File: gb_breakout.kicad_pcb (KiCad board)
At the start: 2 copper layers, 51 x 60.7 mm, 14 parts, among them IC1 74ALVC164245DGG_11, IC2 74ALVC164245DGG_11, J1 Conn_02x16_Counter_Clockwise, U1 Cartridge_Bus

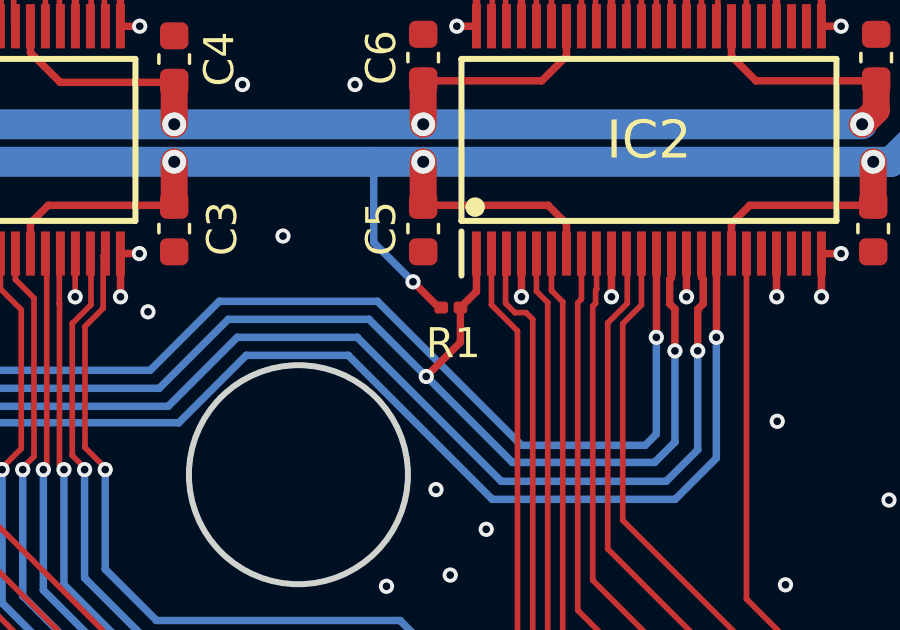
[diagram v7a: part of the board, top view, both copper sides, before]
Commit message: change 0201 resistor to 0402, woops
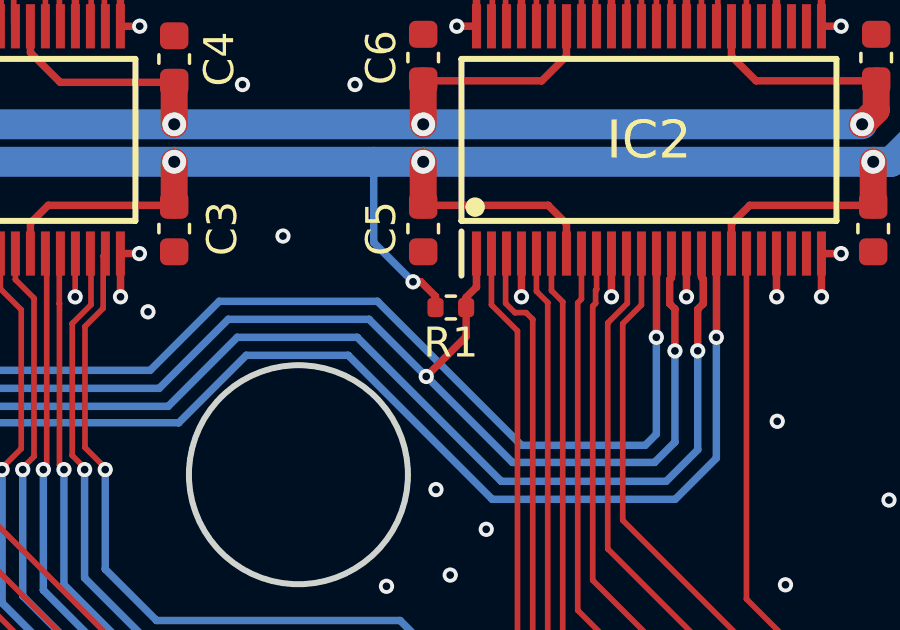
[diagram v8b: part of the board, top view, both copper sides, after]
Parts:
- R1: footprint Resistor_SMD:R_0201_0603Metric -> Resistor_SMD:R_0402_1005Metric
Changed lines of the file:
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@@
     (pad_to_mask_clearance 0)
     (pcbplotparams
-      (layerselection 0x00010fc_ffffffff)
+      (layerselection 0x00010f0_ffffffff)
       (disableapertmacros false)
-      (usegerberextensions false)
+      (usegerberextensions true)
       (usegerberattributes true)
       (usegerberadvancedattributes true)
@@
       (psa4output false)
       (plotreference true)
-      (plotvalue true)
+      (plotvalue false)
       (plotinvisibletext false)
       (sketchpadsonfab false)
@@
       (outputformat 1)
       (mirror false)
-      (drillshape 1)
+      (drillshape 0)
       (scaleselection 1)
       (outputdirectory "")
@@
     )
   )
-  (footprint "Resistor_SMD:R_0201_0603Metric" (layer "F.Cu")
+  (footprint "Resistor_SMD:R_0402_1005Metric" (layer "F.Cu")
     (at 147.32 102.108 180)
-    (descr "Resistor SMD 0201 (0603 Metric), square (rectangular) end terminal, IPC_7351 nominal, (Body size source: https://www.vishay.com/docs/20052/crcw0201e3.pdf), generated with kicad-footprint-generator")
+    (descr "Resistor SMD 0402 (1005 Metric), square (rectangular) end terminal, IPC_7351 nominal, (Body size source: IPC-SM-782 page 72, https://www.pcb-3d.com/wordpress/wp-content/uploads/ipc-sm-782a_amendment_1_and_2.pdf), generated with kicad-footprint-generator")
     (tags "resistor")
     (property "Sheetfile" "gb_breakout.kicad_sch")
     (property "Sheetname" "")
     (attr smd)
-    (fp_text reference "R1" (at -0.08 -1.192) (layer "F.SilkS")
+    (fp_text reference "R1" (at 0 -1.17 180) (layer "F.SilkS")
       (effects (font (size 1 1) (thickness 0.15)))
     )
-    (fp_text value "1k" (at 0 1.05) (layer "F.Fab") hide
+    (fp_text value "1k" (at 0 1.17 180) (layer "F.Fab")
       (effects (font (size 1 1) (thickness 0.15)))
     )
-    (fp_text user "${REFERENCE}" (at 0 -0.68) (layer "F.Fab")
-      (effects (font (size 0.25 0.25) (thickness 0.04)))
+    (fp_text user "${REFERENCE}" (at 0 0 180) (layer "F.Fab")
+      (effects (font (size 0.26 0.26) (thickness 0.04)))
     )
-    (fp_line (start -0.7 0.35) (end -0.7 -0.35) (layer "F.CrtYd") (width 0.05))
-    (fp_line (start 0.7 0.35) (end -0.7 0.35) (layer "F.CrtYd") (width 0.05))
-    (fp_line (start 0.7 -0.35) (end 0.7 0.35) (layer "F.CrtYd") (width 0.05))
-    (fp_line (start -0.7 -0.35) (end 0.7 -0.35) (layer "F.CrtYd") (width 0.05))
-    (fp_line (start -0.3 -0.15) (end 0.3 -0.15) (layer "F.Fab") (width 0.1))
-    (fp_line (start -0.3 0.15) (end -0.3 -0.15) (layer "F.Fab") (width 0.1))
-    (fp_line (start 0.3 0.15) (end -0.3 0.15) (layer "F.Fab") (width 0.1))
-    (fp_line (start 0.3 -0.15) (end 0.3 0.15) (layer "F.Fab") (width 0.1))
-    (pad "" smd roundrect (at 0.345 0 180) (size 0.318 0.36) (layers "F.Paste") (roundrect_rratio 0.25))
-    (pad "" smd roundrect (at -0.345 0 180) (size 0.318 0.36) (layers "F.Paste") (roundrect_rratio 0.25))
-    (pad "1" smd roundrect (at -0.32 0 180) (size 0.46 0.4) (layers "F.Cu" "F.Mask") (roundrect_rratio 0.25)
+    (fp_line (start -0.153641 -0.38) (end 0.153641 -0.38) (layer "F.SilkS") (width 0.12))
+    (fp_line (start -0.153641 0.38) (end 0.153641 0.38) (layer "F.SilkS") (width 0.12))
+    (fp_line (start 0.93 -0.47) (end 0.93 0.47) (layer "F.CrtYd") (width 0.05))
+    (fp_line (start -0.93 0.47) (end -0.93 -0.47) (layer "F.CrtYd") (width 0.05))
+    (fp_line (start 0.93 0.47) (end -0.93 0.47) (layer "F.CrtYd") (width 0.05))
+    (fp_line (start -0.93 -0.47) (end 0.93 -0.47) (layer "F.CrtYd") (width 0.05))
+    (fp_line (start 0.525 -0.27) (end 0.525 0.27) (layer "F.Fab") (width 0.1))
+    (fp_line (start -0.525 -0.27) (end 0.525 -0.27) (layer "F.Fab") (width 0.1))
+    (fp_line (start 0.525 0.27) (end -0.525 0.27) (layer "F.Fab") (width 0.1))
+    (fp_line (start -0.525 0.27) (end -0.525 -0.27) (layer "F.Fab") (width 0.1))
+    (pad "1" smd roundrect (at -0.51 0 180) (size 0.54 0.64) (layers "F.Cu" "F.Paste" "F.Mask") (roundrect_rratio 0.25)
       (net 49 "GB_~{WR}") (pintype "passive"))
-    (pad "2" smd roundrect (at 0.32 0 180) (size 0.46 0.4) (layers "F.Cu" "F.Mask") (roundrect_rratio 0.25)
+    (pad "2" smd roundrect (at 0.51 0 180) (size 0.54 0.64) (layers "F.Cu" "F.Paste" "F.Mask") (roundrect_rratio 0.25)
       (net 32 "+5V") (pintype "passive"))
-    (model "${KICAD6_3DMODEL_DIR}/Resistor_SMD.3dshapes/R_0201_0603Metric.wrl"
+    (model "${KICAD6_3DMODEL_DIR}/Resistor_SMD.3dshapes/R_0402_1005Metric.wrl"
       (offset (xyz 0 0 0))
       (scale (xyz 1 1 1))
@@
     (fp_arc (start 25.5 -5.35) (mid 25.353553 -4.996447) (end 25 -4.85) (layer "Edge.Cuts") (width 0.2))
     (fp_arc (start -24.95 -4.85) (mid -24.773223 -4.776777) (end -24.7 -4.6) (layer "Edge.Cuts") (width 0.2))
-    (fp_arc (start 24.700002 2.449998) (mid 24.260974 3.510789) (end 23.200441 3.950435) (layer "Edge.Cuts") (width 0.2))
+    (fp_arc (start 24.700002 2.449998) (mid 24.260973 3.510786) (end 23.200441 3.950435) (layer "Edge.Cuts") (width 0.2))
     (fp_circle (center 0 -36.7) (end 1.1 -36.7) (layer "Edge.Cuts") (width 0.2) (fill none))
     (fp_circle (center 0 -11.7) (end 3.65 -11.7) (layer "Edge.Cuts") (width 0.2) (fill none))
@@
   (segment (start 127.806 99.311478) (end 127.194522 98.7) (width 0.25) (layer "F.Cu") (net 32))
   (segment (start 127.806 100.308) (end 127.806 99.311478) (width 0.25) (layer "F.Cu") (net 32))
-  (segment (start 146.918 102.108) (end 146.06 101.25) (width 0.25) (layer "F.Cu") (net 32))
+  (segment (start 146.81 101.735) (end 146.81 102.108) (width 0.25) (layer "F.Cu") (net 32))
   (segment (start 156.674 99.311478) (end 157.285478 98.7) (width 0.25) (layer "F.Cu") (net 32))
+  (segment (start 146.06 101.25) (end 146.325 101.25) (width 0.25) (layer "F.Cu") (net 32))
   (segment (start 118.75 116.69) (end 118.74 116.7) (width 0.25) (layer "F.Cu") (net 32))
   (segment (start 123 97.25) (end 123 98.7) (width 0.9) (layer "F.Cu") (net 32))
@@
   (segment (start 127.194522 98.7) (end 123 98.7) (width 0.25) (layer "F.Cu") (net 32))
   (segment (start 118.75 115.6) (end 118.74 115.61) (width 1) (layer "F.Cu") (net 32))
+  (segment (start 146.325 101.25) (end 146.81 101.735) (width 0.25) (layer "F.Cu") (net 32))
   (segment (start 138.1 98.7) (end 138.1 97.25) (width 0.9) (layer "F.Cu") (net 32))
   (segment (start 160.525 66.35) (end 160.525 68.592) (width 1) (layer "F.Cu") (net 32))
@@
   (segment (start 151.174 100.308) (end 151.174 99.311478) (width 0.25) (layer "F.Cu") (net 32))
   (segment (start 151.174 99.311478) (end 150.562522 98.7) (width 0.25) (layer "F.Cu") (net 32))
-  (segment (start 147 102.108) (end 146.918 102.108) (width 0.25) (layer "F.Cu") (net 32))
   (segment (start 118.74 116.7) (end 118.74 116.85) (width 0.25) (layer "F.Cu") (net 32))
   (via (at 138.1 97.25) (size 0.8) (drill 0.4) (layers "F.Cu" "B.Cu") (net 32))
@@
   (segment (start 137.51 112.54) (end 135.8 110.83) (width 0.25) (layer "B.Cu") (net 48))
   (segment (start 154.616489 101.173511) (end 154.674 101.116) (width 0.25) (layer "F.Cu") (net 49))
-  (segment (start 148.174 101.574) (end 147.64 102.108) (width 0.25) (layer "F.Cu") (net 49))
-  (segment (start 147.64 103.265066) (end 147.64 102.108) (width 0.25) (layer "F.Cu") (net 49))
+  (segment (start 147.83 102.108) (end 147.83 103.075066) (width 0.25) (layer "F.Cu") (net 49))
+  (segment (start 147.83 101.77) (end 148.175 101.425) (width 0.25) (layer "F.Cu") (net 49))
   (segment (start 154.79 102.154855) (end 154.616489 101.981344) (width 0.25) (layer "F.Cu") (net 49))
+  (segment (start 147.83 102.108) (end 147.83 101.77) (width 0.25) (layer "F.Cu") (net 49))
   (segment (start 154.79 103.552993) (end 154.79 102.154855) (width 0.25) (layer "F.Cu") (net 49))
-  (segment (start 148.174 100.308) (end 148.174 101.574) (width 0.25) (layer "F.Cu") (net 49))
   (segment (start 154.616489 101.981344) (end 154.616489 101.173511) (width 0.25) (layer "F.Cu") (net 49))
+  (segment (start 147.83 103.075066) (end 146.5 104.405066) (width 0.25) (layer "F.Cu") (net 49))
+  (segment (start 148.175 101.425) (end 148.174 101.424) (width 0.25) (layer "F.Cu") (net 49))
+  (segment (start 148.174 101.424) (end 148.174 100.308) (width 0.25) (layer "F.Cu") (net 49))
   (segment (start 154.674 101.116) (end 154.674 100.308) (width 0.25) (layer "F.Cu") (net 49))
   (segment (start 121.988125 115.897451) (end 121.988125 116.928125) (width 0.25) (layer "F.Cu") (net 49))
-  (segment (start 146.5 104.405066) (end 147.64 103.265066) (width 0.25) (layer "F.Cu") (net 49))
   (segment (start 121.988125 116.928125) (end 121.99 116.93) (width 0.25) (layer "F.Cu") (net 49))
   (via (at 146.5 104.405066) (size 0.508) (drill 0.254) (layers "F.Cu" "B.Cu") (net 49))
